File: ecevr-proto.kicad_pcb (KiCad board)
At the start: 4 copper layers, 100 x 100 mm, 393 parts, among them J1 CUR_SEL, J19 SFP, J2 PEN_SEL, J20 SFP_CAGE, J2001 BNC, J2051 BNC, J2201 BEL_0845_2G1T_H5, J3 USB_C_Receptacle_USB2.0, J4 JTAG, Q1 SSM6N35AFE, Q2 SSM6N35AFE, Q3 Si3477, Q4 SSM6N35AFE, Q5 SSM6N35AFE, Q6 Si3477, Q7 SSM6N35AFE, SW1 PROG, SW2101 SW_DIP_x08, U1 XC7A35T-CSG325, U10 74LVC1G06, U11 UTC2000, U12 5P49V6965, U13 TPS3808DBV, U14 74LVC1G06, U15 74LVC2T45DC, U16 74LVC2T45DC, U17 74LVC06, U18 74LVC1T126, U19 74AHC1T86, U2 AT25SL641, U20 74AHC1T86, U2001 74LVC2T45DC, U2051 74LVC2T45DC, U21 74LVC1G06, U2101 74AHC1T86, U2102 74AHC1T86, U2103 PCA9306, U2104 24FC16T, U2105 74AHC1T86, U2106 74AHC1T86, U22 74AC126, U2201 74AHC1T86, U2202 74LVC1G06, U2301 lan9254, U3 FT240XQ, U4 TLV62569ADDC, U5 TPS62A01A-SOT563, U6 TPS62A01A-SOT563, U7 TLV62569ADDC, U8 74ALVC125, U9 TLV62569ADDC, X2301 FNETHE025, Y1 25MHz

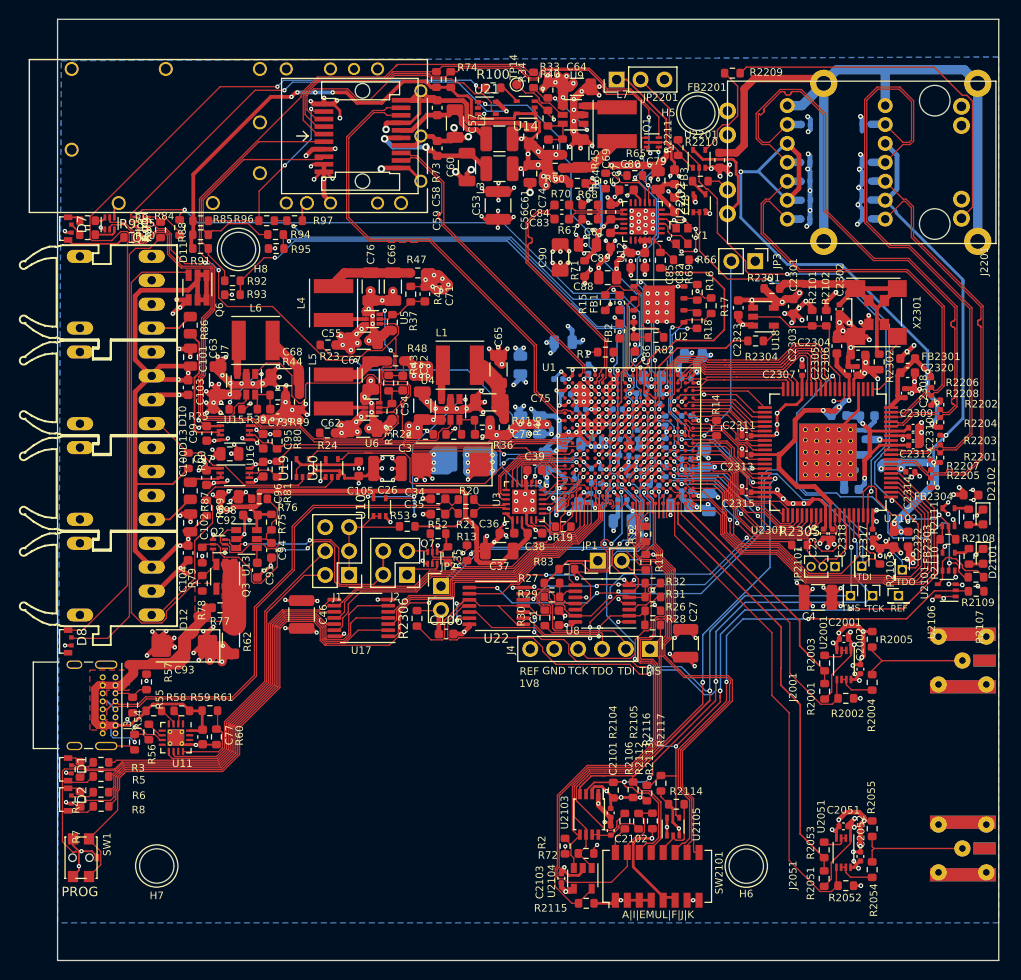
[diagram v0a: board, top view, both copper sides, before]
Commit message: PCB: updated USBC-connector footprint, rearranged REF silkscreen text
UCBC annular rings increased in size (for EuroCircuits)
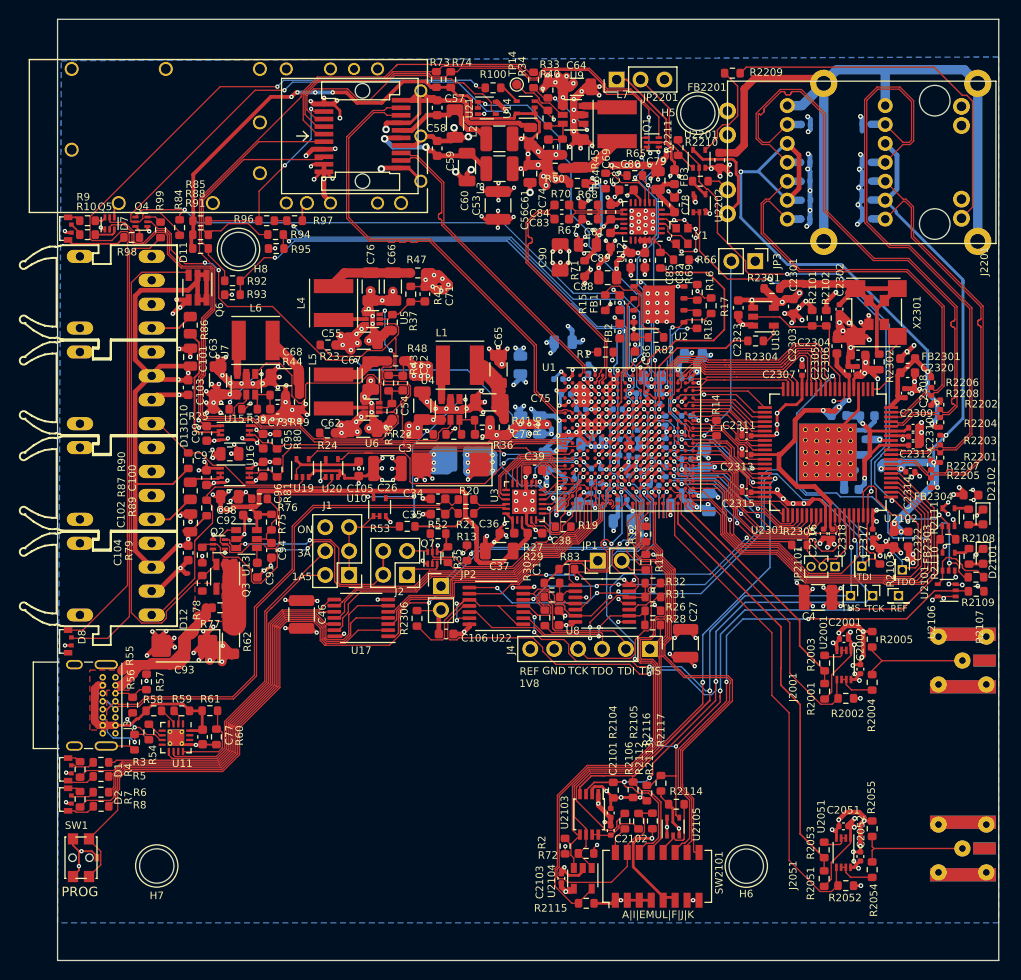
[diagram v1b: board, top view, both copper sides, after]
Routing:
- net Net-(R4-Pad1): track 56.8 -> 41.6 mm
- net VBUS: track 45.6 -> 48.9 mm
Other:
- board text added: "1A5"
- board text added: "3A"
- board text added: "ON"

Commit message: added 3rd GPIO
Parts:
- removed TP5, TP8: Dummy End, proj_footprints:endpoint_0.1mm
- added C2003: 100n, Capacitor_SMD:C_0402_1005Metric, F.Cu at (183.5, 113.8)
- added C2004: 100n, Capacitor_SMD:C_0402_1005Metric, F.Cu at (185.3, 117.0)
- added J2002: BNC, proj_footprints:LEMO+SMA, F.Cu at (196.1, 116.1)
- added R2006: 100k, Resistor_SMD:R_0603_1608Metric, F.Cu at (181.4, 119.3)
- added R2007: 3k3, Resistor_SMD:R_0603_1608Metric, F.Cu at (183.8, 120.1)
- added R2008: 100, Resistor_SMD:R_0603_1608Metric, F.Cu at (181.4, 116.3)
- added R2009: 0, Resistor_SMD:R_0603_1608Metric, F.Cu at (186.6, 118.4)
- added R2010: 100k, Resistor_SMD:R_0603_1608Metric, F.Cu at (186.6, 114.0)
- added U2002: 74LVC2T45DC, Package_SO:VSSOP-8_2.3x2mm_P0.5mm, F.Cu at (183.5, 116.6)
- moved C2051 8.97 mm to (183.5, 102.8)
- moved C2052 8.97 mm to (185.3, 106.0)
- moved J2051 8.97 mm to (196.1, 105.1)
- moved R2051 8.97 mm to (181.4, 108.3)
- moved R2052 8.97 mm to (183.8, 109.1)
- moved R2053 8.97 mm to (181.4, 105.3)
- moved R2054 8.97 mm to (186.6, 107.4)
- moved R2055 8.97 mm to (186.6, 103.0)
- moved U2051 8.97 mm to (183.5, 105.6)
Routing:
- net IO_L20N_T3_A07_D23_14: track 1.53 -> 54.5 mm
- net IO_L17P_T2_A14_D30_14: track 2.52 -> 49.1 mm
- net Net-(J2002-Pad1): track 0.00 -> 12.3 mm
- net GND: track 693.5 -> 704.7 mm, vias 392 -> 398
- net +3V3: track 163.2 -> 152.3 mm, vias 34 -> 36
- net +1V8: track 333.8 -> 343.6 mm, vias 120 -> 122
- net IO_L18P_T2_A12_D28_14: track 45.5 -> 36.6 mm
- net IO_L17N_T2_A13_D29_14: track 53.0 -> 44.0 mm
- net Net-(R2009-Pad1): track 0.00 -> 3.92 mm
- net Net-(R2008-Pad2): track 0.00 -> 2.96 mm
- net Net-(J2001-Pad1): track 12.4 -> 12.9 mm

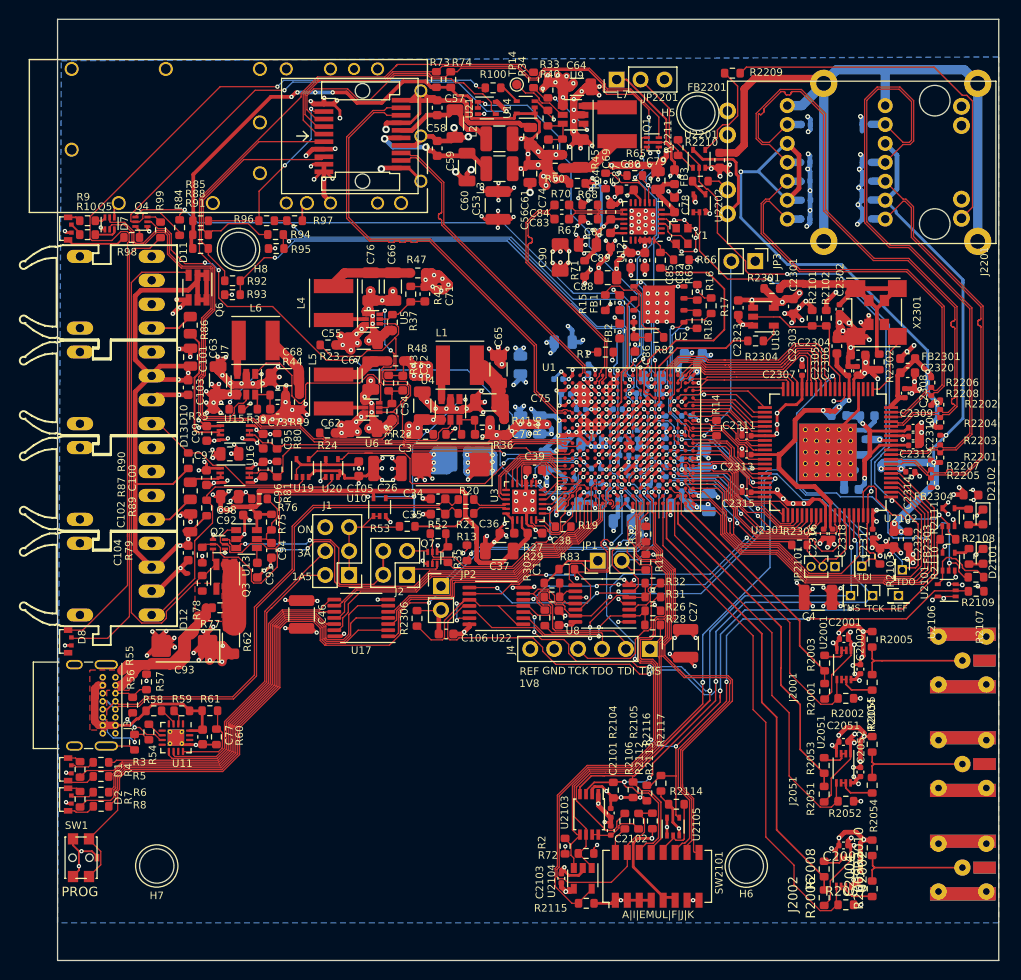
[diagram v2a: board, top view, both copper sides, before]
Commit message: Added pull-up resistor to lan9254 #RST line
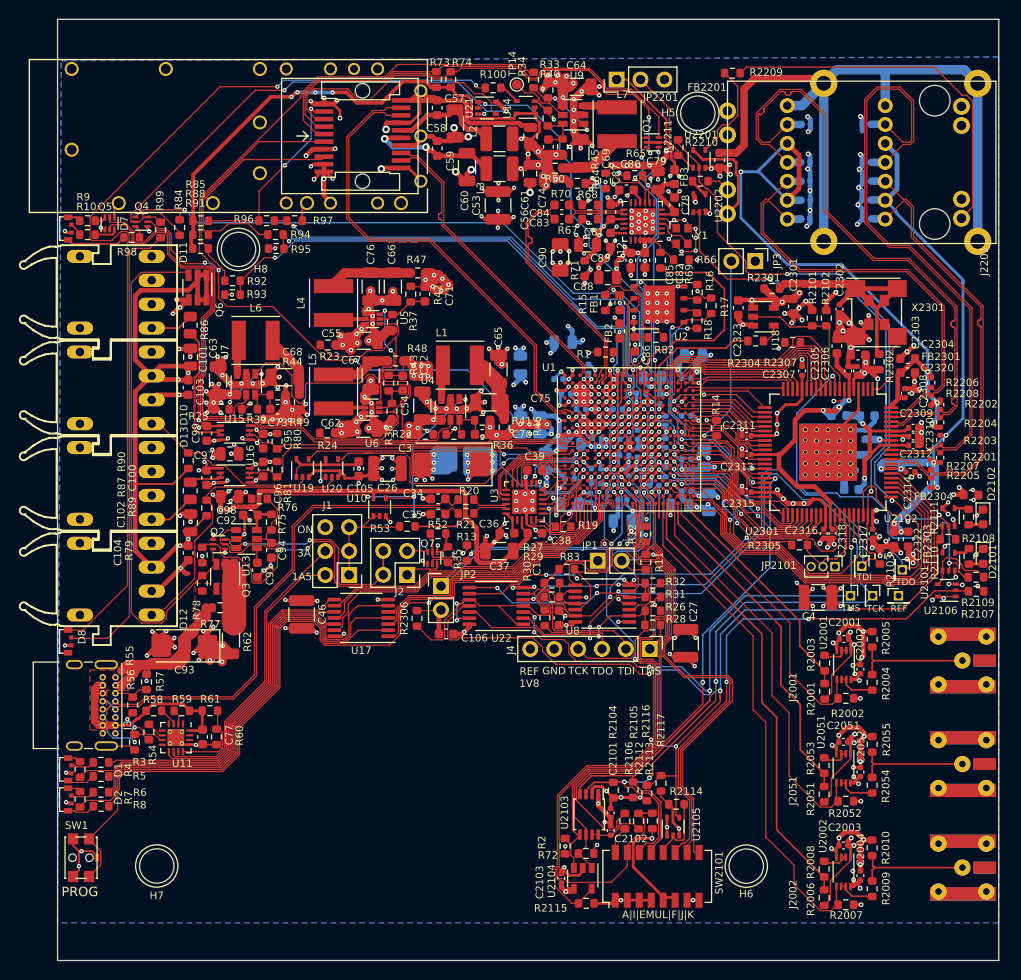
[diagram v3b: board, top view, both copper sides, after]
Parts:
- added R2307: 10k, Resistor_SMD:R_0603_1608Metric, F.Cu at (178.1, 60.3)
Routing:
- net IO_L8N_T1_AD10N_15: track 23.8 -> 25.0 mm
- net +1V8: track 343.6 -> 344.5 mm, vias 122 -> 123

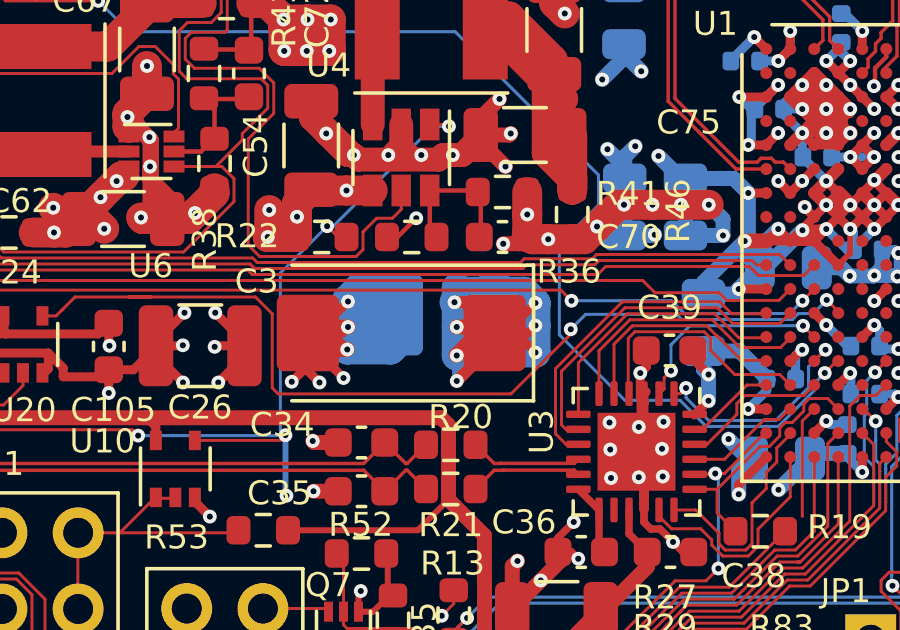
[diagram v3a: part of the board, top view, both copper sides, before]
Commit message: updated cap footprint
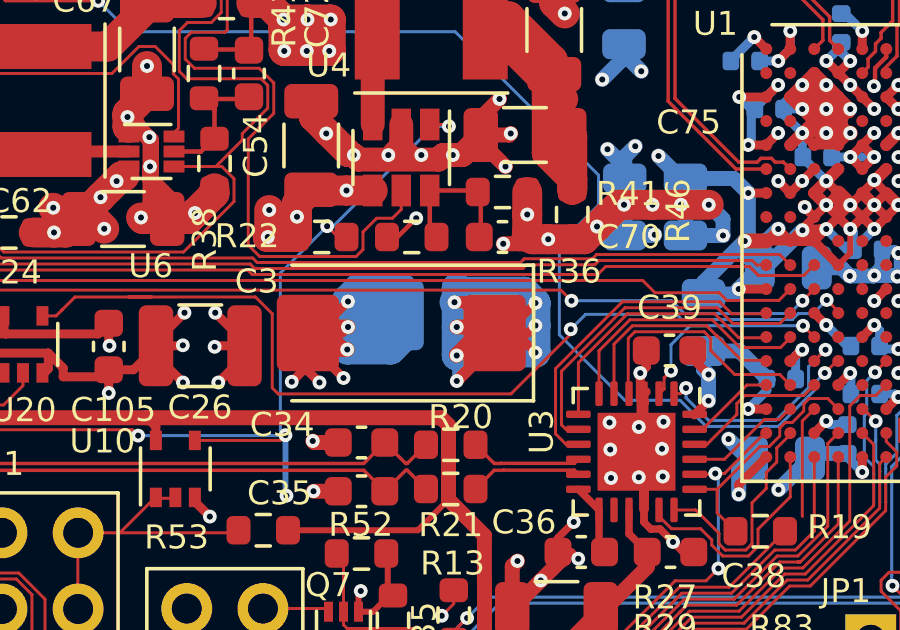
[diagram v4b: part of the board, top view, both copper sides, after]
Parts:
- C21: footprint proj_footprints:C_pol_1210_3225Metric -> Capacitor_Tantalum_SMD:CP_EIA-3528-15_AVX-H
- J2001, J2002, J2051: value BNC -> IO_CONN
